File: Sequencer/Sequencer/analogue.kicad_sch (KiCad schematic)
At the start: 18 parts, among them U10 TL074, U11 TL072, U12 LM285Z-ADJ, U9 CD74HC4067M

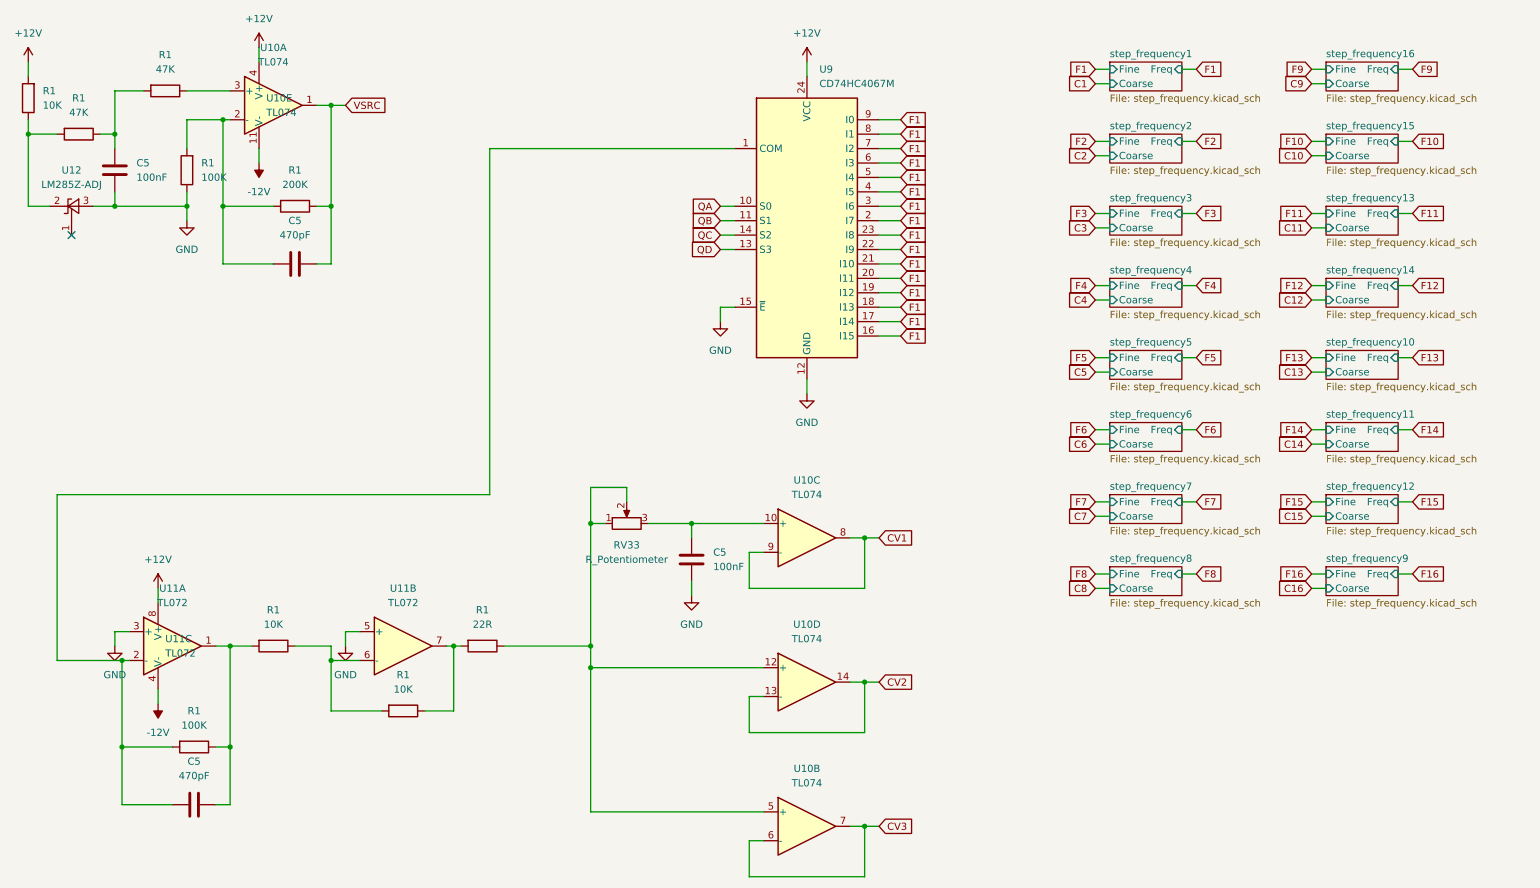
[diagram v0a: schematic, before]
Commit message: Sequencer - minor progress on routing
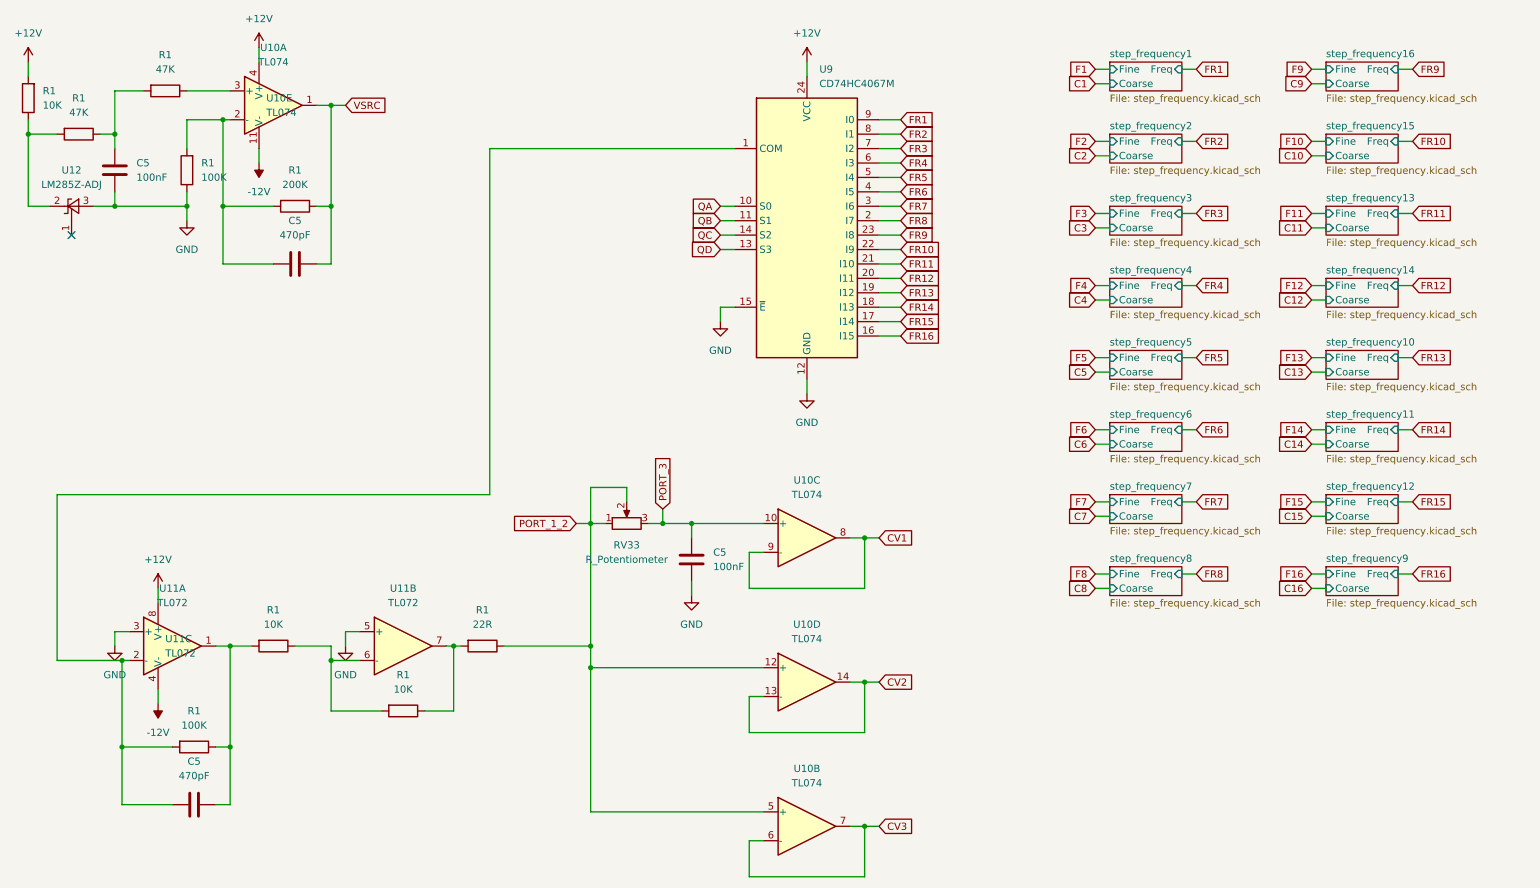
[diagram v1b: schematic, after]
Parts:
- C5: footprint Capacitor_THT:C_Disc_D3.0mm_W1.6mm_P2.50mm -> Capacitor_THT:C_Disc_D5.0mm_W2.5mm_P2.50mm
- R1: footprint Resistor_THT:R_Axial_DIN0207_L6.3mm_D2.5mm_P7.62mm_Horizontal -> Library:R_Axial_DIN0207_L6.3mm_D2.5mm_P7.62mm_Horizontal
- U9: footprint Package_SO:SOIC-24W_7.5x15.4mm_P1.27mm -> Package_DIP:DIP-24_W15.24mm_Socket_LongPads
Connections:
- net F1: no longer U9.16 (I15), U9.17 (I14), U9.18 (I13), U9.19 (I12), U9.2 (I7), U9.20 (I11), U9.21 (I10), U9.22 (I9), U9.23 (I8), U9.3 (I6), U9.4 (I5), U9.5 (I4), U9.6 (I3), U9.7 (I2), U9.8 (I1), U9.9 (I0)
- net PORT_1_2: now reaches R1.1, RV33.1, RV33.2, U10.12 (+), U10.5 (+)
- net PORT_3: now reaches C5.2, RV33.3, U10.10 (+)
- new net FR1: U9.9 (I0)
- new net FR10: U9.22 (I9)
- new net FR11: U9.21 (I10)
- new net FR12: U9.20 (I11)
- new net FR13: U9.19 (I12)
- new net FR14: U9.18 (I13)
- new net FR15: U9.17 (I14)
- new net FR16: U9.16 (I15)
- new net FR2: U9.8 (I1)
- new net FR3: U9.7 (I2)
- new net FR4: U9.6 (I3)
- new net FR5: U9.5 (I4)
- new net FR6: U9.4 (I5)
- new net FR7: U9.3 (I6)
- new net FR8: U9.2 (I7)
- new net FR9: U9.23 (I8)
